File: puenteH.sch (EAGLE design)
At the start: 20 parts, among them IC1 LM393N, Q1 IRF4905, Q2 IRLZ44Z, Q3 IRLZ44Z, Q4 IRF4905, Q5 IRF540, Q6 IRF540, Q7 IRF9530, Q8 IRF9530

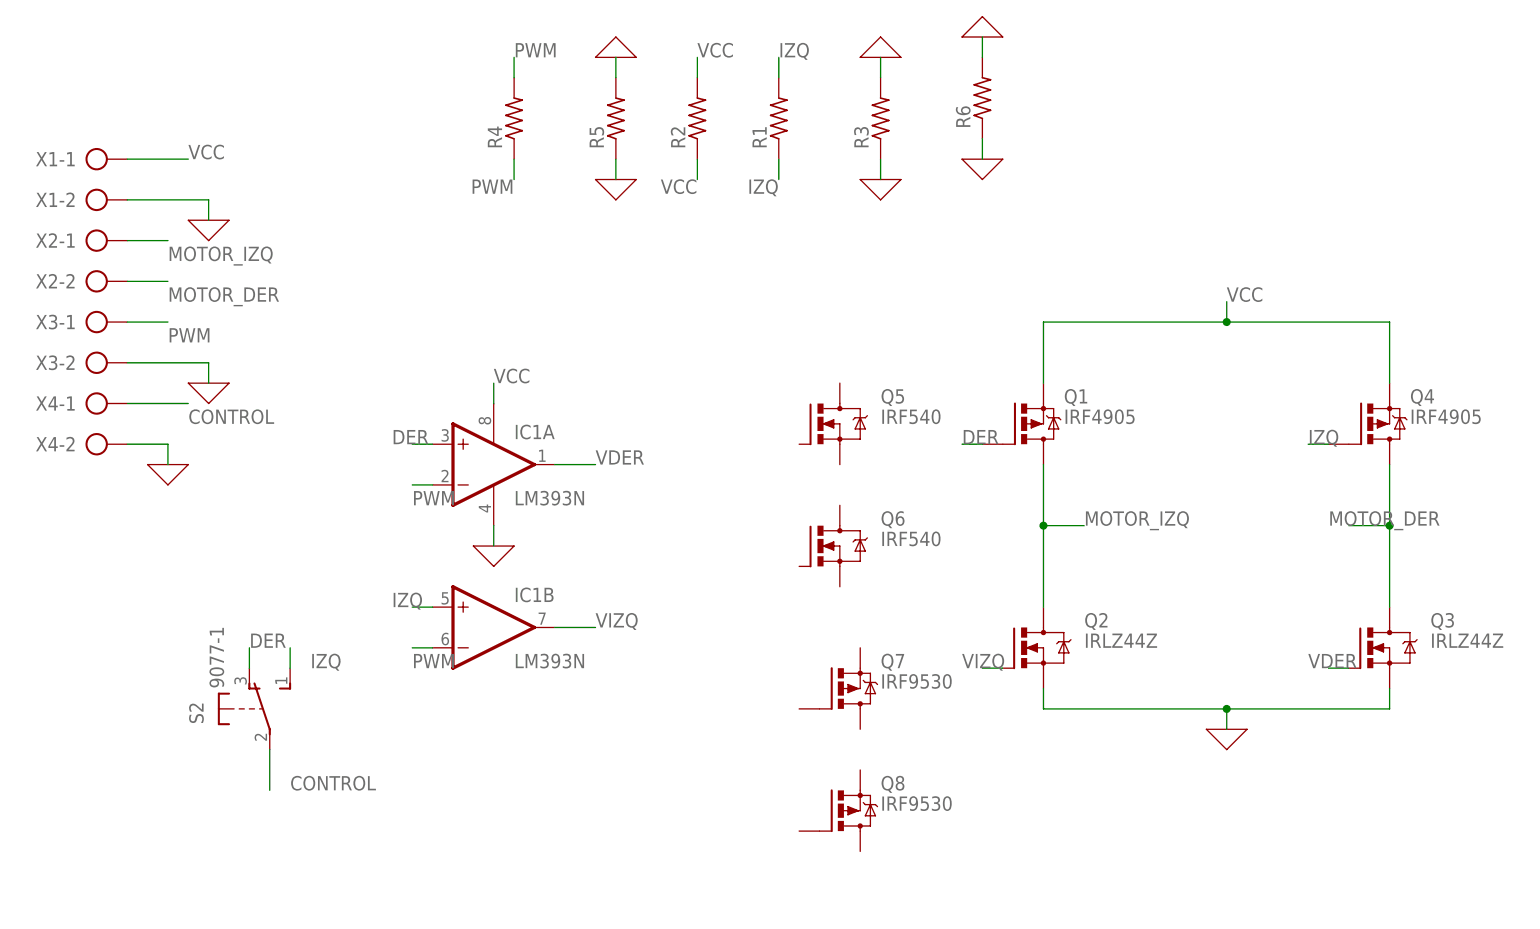
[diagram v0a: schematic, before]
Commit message: Board using real components ready, just need to verify that they in fact exist (or that it is possible to find them at the store)
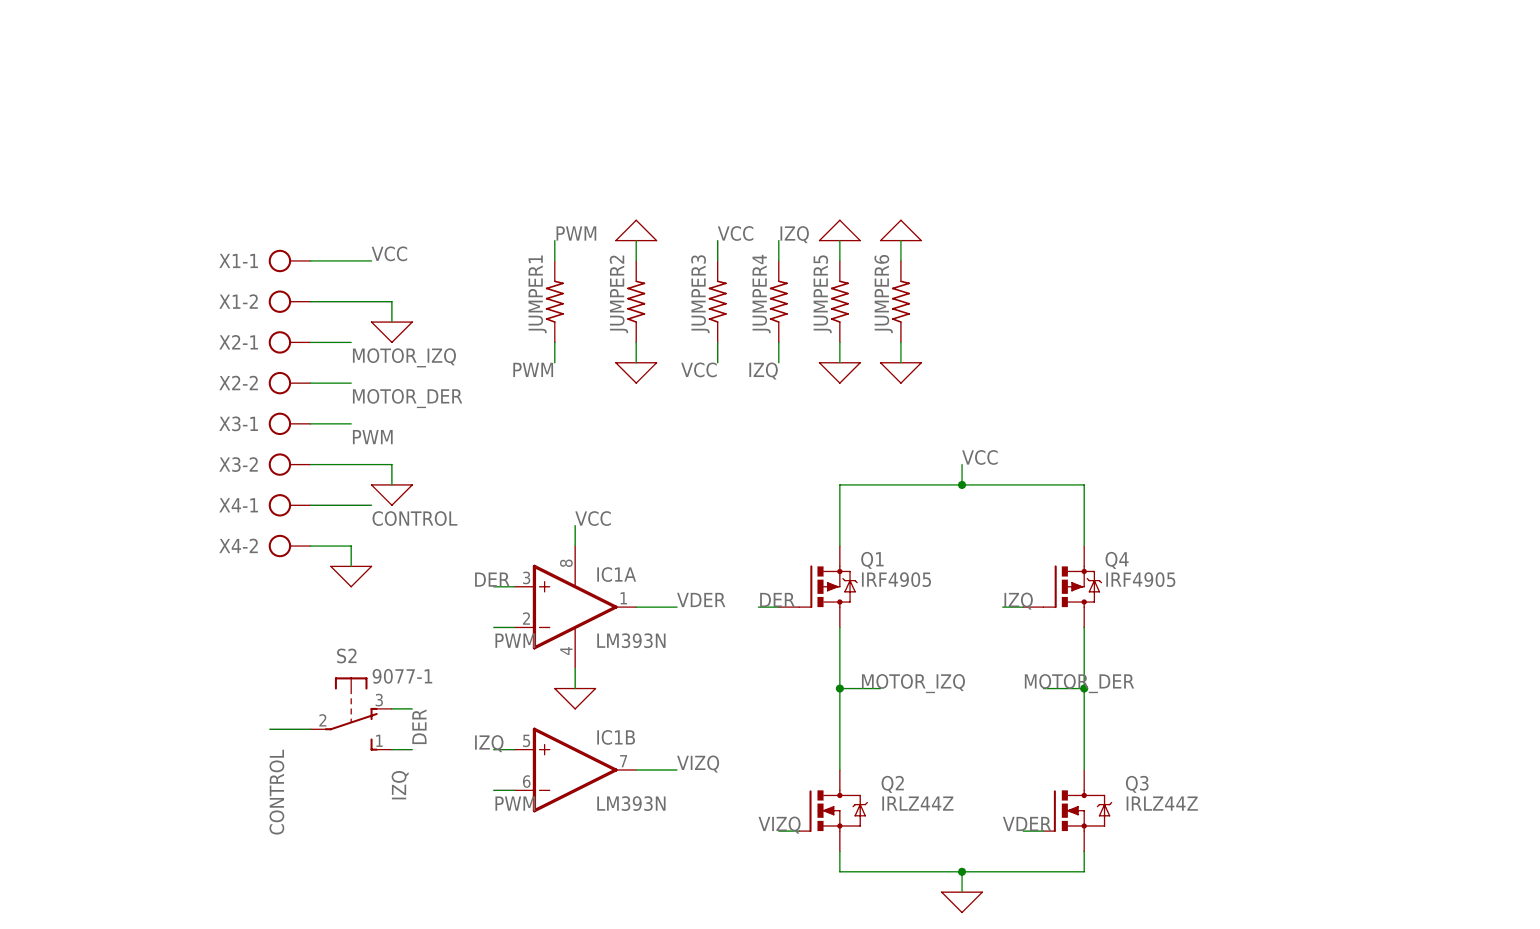
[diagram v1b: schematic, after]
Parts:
- removed Q5, Q6: IRF540, transistor-power:IRF540
- removed Q7, Q8: IRF9530, transistor-power:IRF9530
- removed R1, R5: (no value), rcl:R-US_0204/7
- removed R2, R3, R4, R6: (no value), rcl:R-US_0204/5
- added JUMPER1, JUMPER3, JUMPER5: (no value), rcl:R-US_0204/5
- added JUMPER2, JUMPER4, JUMPER6: (no value), rcl:R-US_0204/7
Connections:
- net 0: now also JUMPER2.1, JUMPER2.2, JUMPER5.1, JUMPER5.2, JUMPER6.1, JUMPER6.2; no longer R3.1, R3.2, R5.1, R5.2, R6.1, R6.2
- net IZQ: now also JUMPER4.1, JUMPER4.2; no longer R1.1, R1.2
- net PWM: now also JUMPER1.1, JUMPER1.2; no longer R4.1, R4.2
- net VCC: now also JUMPER3.1, JUMPER3.2; no longer R2.1, R2.2
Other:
- moved on the sheet: IC1A, IC1B, Q1, Q2, Q3, Q4, S2, X1-1, X1-2, X2-1, X2-2, X3-1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
